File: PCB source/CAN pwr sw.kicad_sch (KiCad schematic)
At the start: 17 parts, among them Q3 AO3401A, Q8 AO3400A, Q9 AO3401A

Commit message: production ready
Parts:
- removed C3: 22uF, PCM_JLCPCB:C_0603, symbol PCM_JLCPCB-Capacitors:0603,22uF
- removed D2: MCR100-6, Package_TO_SOT_SMD:SOT-23, symbol Device:Q_SCR_KAG
- removed Q9: AO3401A, PCM_JLCPCB:Q_SOT-23, symbol PCM_JLCPCB-Transistors:PMOS,AO3401A
- removed R49: 1kΩ, PCM_JLCPCB:R_0402, symbol PCM_JLCPCB-Resistors:0402,1kΩ
- removed R50, R51, R52, R53: 100kΩ, PCM_JLCPCB:R_0402, symbol PCM_JLCPCB-Resistors:0402,100kΩ
- removed R54: 22Ω, PCM_JLCPCB:R_0402, symbol PCM_JLCPCB-Resistors:0402,22Ω
- removed R56: 39kΩ, PCM_JLCPCB:R_0402, symbol PCM_JLCPCB-Resistors:0402,39kΩ
- removed TP6: V_GSCR, TestPoint:TestPoint_Pad_D1.0mm, symbol Connector:TestPoint
- removed TP7: V_cap, TestPoint:TestPoint_Pad_D1.0mm, symbol Connector:TestPoint
- removed TP8: Vgate, TestPoint:TestPoint_Pad_D1.0mm, symbol Connector:TestPoint
- removed TP9: Vcan, symbol Connector:TestPoint
- added R47: 10kΩ, PCM_JLCPCB:R_0402, symbol PCM_JLCPCB-Resistors:0402,10kΩ
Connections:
- net at Q8.1 (G): now also R47.2
- new net CAN_3V3_ON: R47.1
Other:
- note added: "3v3 might not be equal different LDO"
- note added: "Avoided using orange GPIO for Q3 because of possible current loop"
- note added: "CAN"
- note added: "RPI"
- note removed: "1V here = 3/4v circuit will turn on only on 1.3v vcap (c3) wich is well above typycal Vgs for Q9 this should prevent turn off without capacitor discharge"
- note removed: "Gate trigger 0.6v Hold 0.5mA"
- note removed: "Improved delay circuit (c) Artem Horiunov"
- note removed: "Vgs = ~1v"
- note removed: "approx 0.45 sec delay"

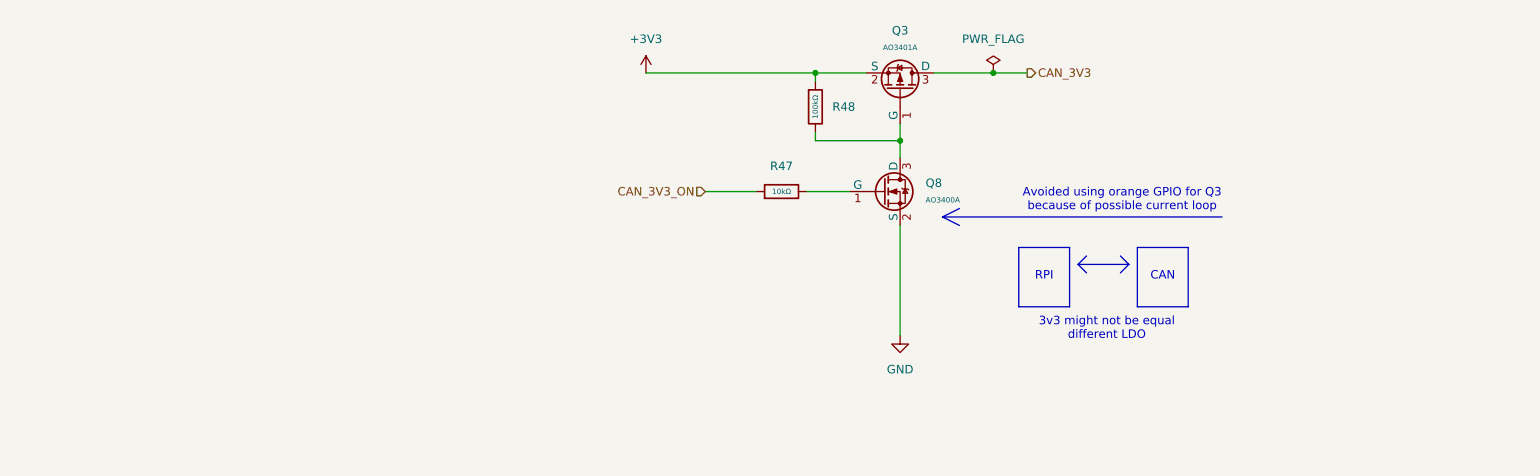
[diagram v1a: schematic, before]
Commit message: Fix can power delivery , fixed placment of the mosfets, CAN power  pull down to avoid DFU boot, added new porgraming connector
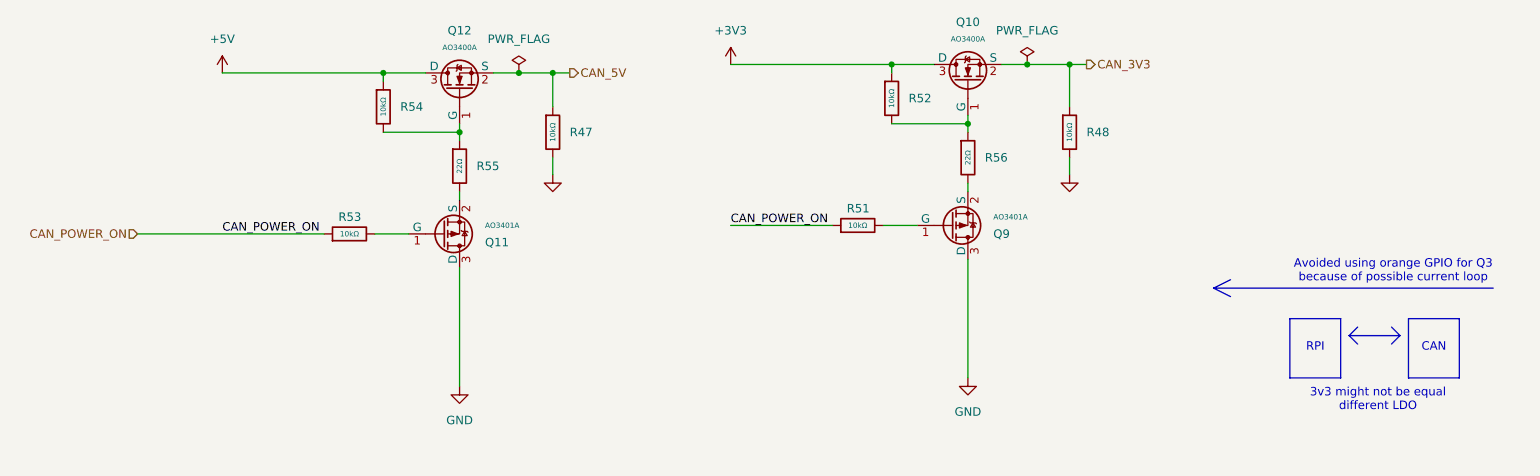
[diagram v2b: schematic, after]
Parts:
- removed Q3: AO3401A, PCM_JLCPCB:Q_SOT-23, symbol PCM_JLCPCB-Transistors:PMOS,AO3401A
- removed Q8: AO3400A, PCM_JLCPCB:Q_SOT-23, symbol PCM_JLCPCB-Transistors:NMOS,AO3400A
- removed R48: 100kΩ, PCM_JLCPCB:R_0402, symbol PCM_JLCPCB-Resistors:0402,100kΩ
- added Q10, Q12: AO3400A, PCM_JLCPCB:Q_SOT-23, symbol PCM_JLCPCB-Transistors:NMOS,AO3400A
- added Q11, Q9: AO3401A, PCM_JLCPCB:Q_SOT-23, symbol PCM_JLCPCB-Transistors:PMOS,AO3401A
- added R48, R51, R52, R53, R54: 10kΩ, PCM_JLCPCB:R_0402, symbol PCM_JLCPCB-Resistors:0402,10kΩ
- added R55, R56: 22Ω, PCM_JLCPCB:R_0402, symbol PCM_JLCPCB-Resistors:0402,22Ω
- R47: Attrition Qty 10 -> 0; Stock 6144808 -> 7508513
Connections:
- net +3V3: now also Q10.3 (D), R52.1
- net CAN_3V3: now also Q10.2 (S), R48.1
- net GND: now also R47.2, Q11.3 (D), Q9.3 (D), R48.2
- net CAN_3V3_ON renamed CAN_5V
- net CAN_5V: now also Q12.2 (S)
- new net: Q11.1 (G), R53.2
- new net: Q9.1 (G), R51.2
- new net: Q12.1 (G), R54.2, R55.1
- new net: Q11.2 (S), R55.2
- new net: Q10.1 (G), R52.2, R56.1
- new net: Q9.2 (S), R56.2
- new net +5V: Q12.3 (D), R54.1
- new net CAN_POWER_ON: R51.1, R53.1
